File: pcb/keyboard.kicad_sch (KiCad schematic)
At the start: 52 parts, among them J1 TRRS, SW11 11, SW12 12, SW13 13, SW14 14, SW15 15, SW16 16, SW17 17, SW18 18, SW19 19, SW21 21, SW22 22, SW23 23, SW24 24, SW25 25, SW26 26, SW27 27, SW28 28, SW29 29, SW31 31, SW32 32, SW33 33, SW34 34, SW35 35, SW36 36, SW37 37, SW38 38, SW39 39, SW41 41, SW42 42, SW43 43, SW45 45, SW46 46, SW47 47, SW48 48, SW49 49, U1 EliteC

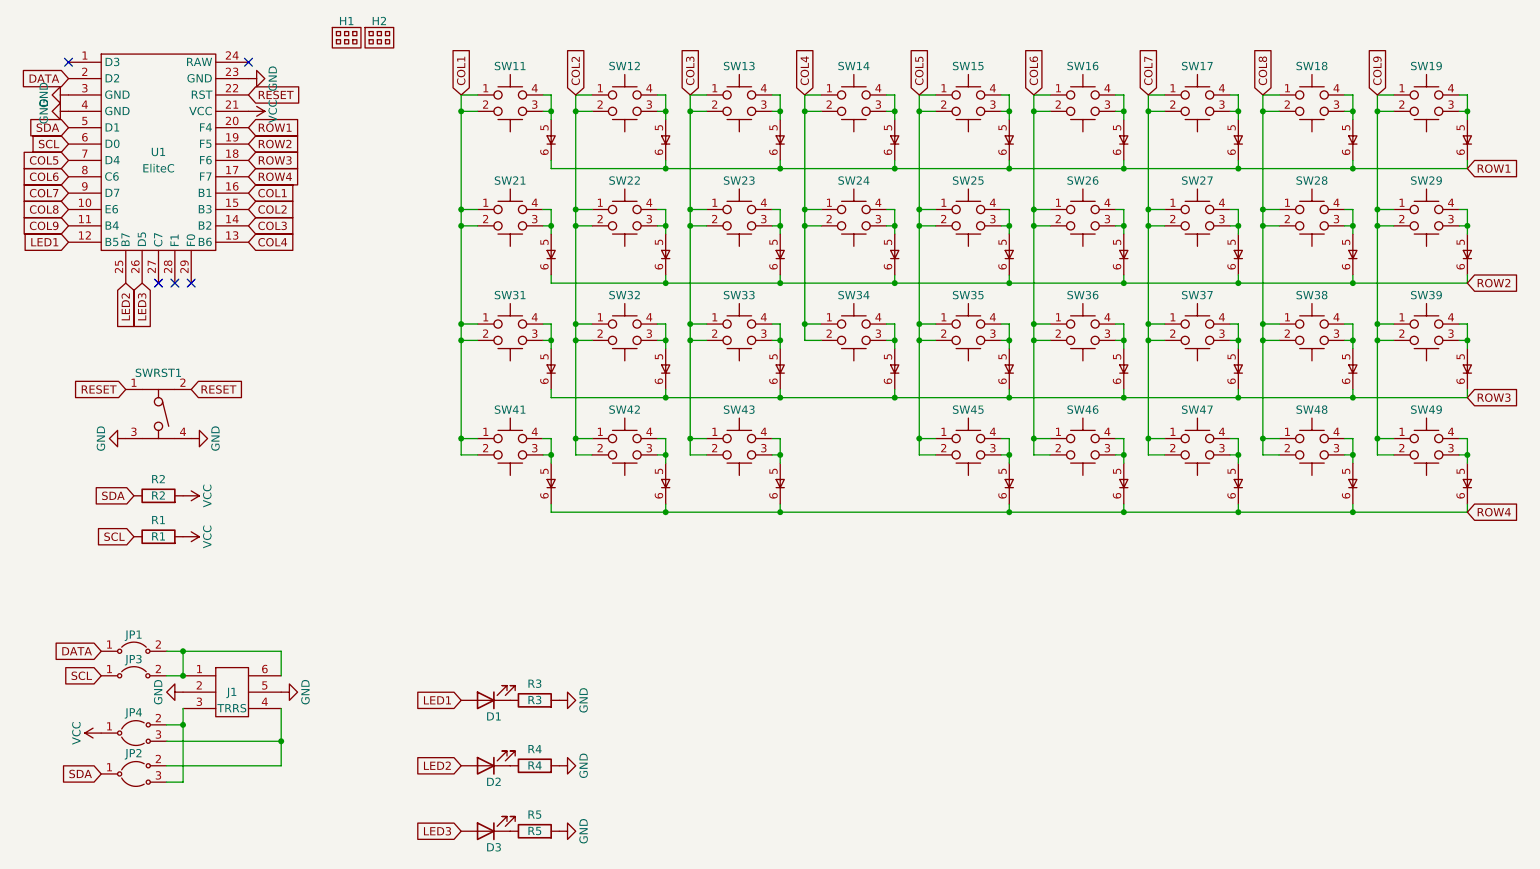
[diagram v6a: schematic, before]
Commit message: update toggling 3D model for left and right sides
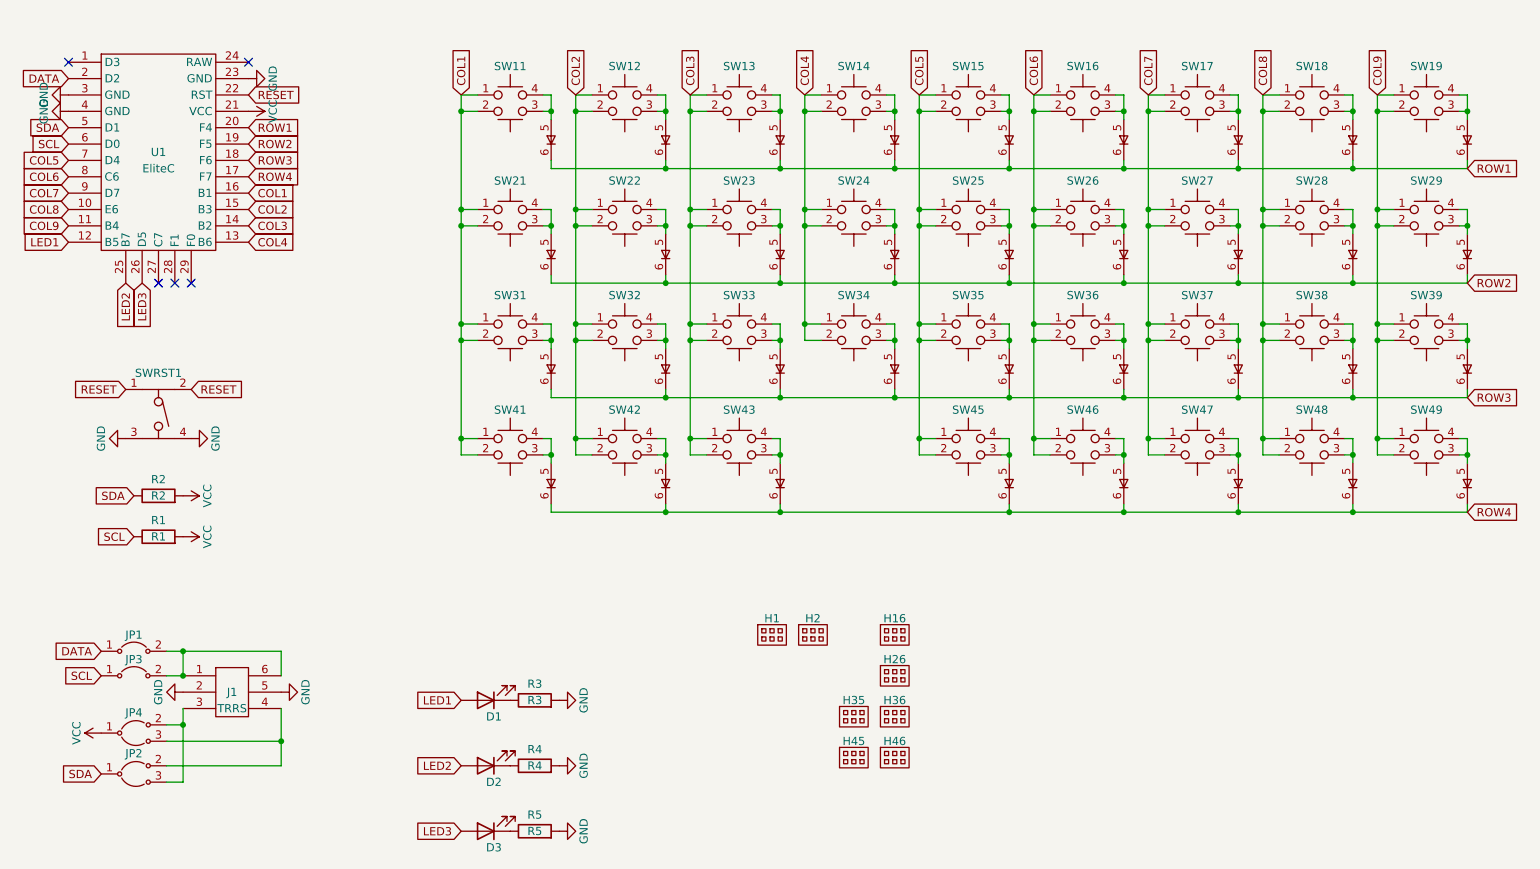
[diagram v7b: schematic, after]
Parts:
- added H16: H16, Keyboard:SwitchDoubleNo3D, symbol Keyboard:Plate
- added H26: H26, Keyboard:SwitchDoubleNo3D, symbol Keyboard:Plate
- added H35: H35, Keyboard:SwitchDoubleNo3D, symbol Keyboard:Plate
- added H36: H36, Keyboard:SwitchDoubleNo3D, symbol Keyboard:Plate
- added H45: H45, Keyboard:SwitchDoubleNo3D, symbol Keyboard:Plate
- added H46: H46, Keyboard:SwitchDoubleNo3D, symbol Keyboard:Plate
- H2: value H1 -> H2
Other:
- moved on the sheet: H1, H2
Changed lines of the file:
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@@
     )
   )
-  (symbol (lib_id "Keyboard:Plate") (at 85.09 30.48 0) (unit 1)
-    (in_bom yes) (on_board yes) (dnp no) (fields_autoplaced)
-    (property "Reference" "H1" (at 85.09 27.94 0) (do_not_autoplace)
-      (effects (font (size 1.27 1.27)))
-    )
-    (property "Value" "H1" (at 84.1375 30.1625 0) (do_not_autoplace)
-      (effects (font (size 1.27 1.27)) hide)
-    )
-    (property "Footprint" "Keyboard:RightPlate" (at 84.1375 30.1625 0)
-      (effects (font (size 1.27 1.27)) hide)
-    )
-    (property "Datasheet" "" (at 84.1375 30.1625 0)
+  (symbol (lib_id "Keyboard:Plate") (at 151.13 123.19 0) (unit 1)
+    (in_bom yes) (on_board yes) (dnp no) (fields_autoplaced)
+    (property "Reference" "H1" (at 151.13 120.65 0) (do_not_autoplace)
+      (effects (font (size 1.27 1.27)))
+    )
+    (property "Value" "H1" (at 150.1775 122.8725 0) (do_not_autoplace)
+      (effects (font (size 1.27 1.27)) hide)
+    )
+    (property "Footprint" "Keyboard:RightPlate" (at 150.1775 122.8725 0)
+      (effects (font (size 1.27 1.27)) hide)
+    )
+    (property "Datasheet" "" (at 150.1775 122.8725 0)
       (effects (font (size 1.27 1.27)) hide)
     )
@@
     )
   )
+  (symbol (lib_id "Keyboard:Plate") (at 170.18 142.24 0) (unit 1)
+    (in_bom yes) (on_board yes) (dnp no) (fields_autoplaced)
+    (property "Reference" "H46" (at 170.18 139.7 0) (do_not_autoplace)
+      (effects (font (size 1.27 1.27)))
+    )
+    (property "Value" "H46" (at 169.2275 141.9225 0) (do_not_autoplace)
+      (effects (font (size 1.27 1.27)) hide)
+    )
+    (property "Footprint" "Keyboard:SwitchDoubleNo3D" (at 169.2275 141.9225 0)
+      (effects (font (size 1.27 1.27)) hide)
+    )
+    (property "Datasheet" "" (at 169.2275 141.9225 0)
+      (effects (font (size 1.27 1.27)) hide)
+    )
+    (instances
+      (project "keyboard"
+        (path "/7807834d-3d77-4d25-b9d8-d933072c7b84"
+          (reference "H46") (unit 1)
+        )
+      )
+    )
+  )
   (symbol (lib_id "Keyboard:Switch") (at 217.17 40.64 0) (unit 1)
     (in_bom yes) (on_board yes) (dnp no) (fields_autoplaced)
@@
     )
   )
+  (symbol (lib_id "Keyboard:Plate") (at 170.18 123.19 0) (unit 1)
+    (in_bom yes) (on_board yes) (dnp no) (fields_autoplaced)
+    (property "Reference" "H16" (at 170.18 120.65 0) (do_not_autoplace)
+      (effects (font (size 1.27 1.27)))
+    )
+    (property "Value" "H16" (at 169.2275 122.8725 0) (do_not_autoplace)
+      (effects (font (size 1.27 1.27)) hide)
+    )
+    (property "Footprint" "Keyboard:SwitchDoubleNo3D" (at 169.2275 122.8725 0)
+      (effects (font (size 1.27 1.27)) hide)
+    )
+    (property "Datasheet" "" (at 169.2275 122.8725 0)
+      (effects (font (size 1.27 1.27)) hide)
+    )
+    (instances
+      (project "keyboard"
+        (path "/7807834d-3d77-4d25-b9d8-d933072c7b84"
+          (reference "H16") (unit 1)
+        )
+      )
+    )
+  )
   (symbol (lib_id "Keyboard:Switch") (at 199.39 76.2 0) (unit 1)
     (in_bom yes) (on_board yes) (dnp no) (fields_autoplaced)
@@
     )
   )
+  (symbol (lib_id "Keyboard:Plate") (at 163.83 135.89 0) (unit 1)
+    (in_bom yes) (on_board yes) (dnp no) (fields_autoplaced)
+    (property "Reference" "H35" (at 163.83 133.35 0) (do_not_autoplace)
+      (effects (font (size 1.27 1.27)))
+    )
+    (property "Value" "H35" (at 162.8775 135.5725 0) (do_not_autoplace)
+      (effects (font (size 1.27 1.27)) hide)
+    )
+    (property "Footprint" "Keyboard:SwitchDoubleNo3D" (at 162.8775 135.5725 0)
+      (effects (font (size 1.27 1.27)) hide)
+    )
+    (property "Datasheet" "" (at 162.8775 135.5725 0)
+      (effects (font (size 1.27 1.27)) hide)
+    )
+    (instances
+      (project "keyboard"
+        (path "/7807834d-3d77-4d25-b9d8-d933072c7b84"
+          (reference "H35") (unit 1)
+        )
+      )
+    )
+  )
+  (symbol (lib_id "Keyboard:Plate") (at 170.18 135.89 0) (unit 1)
+    (in_bom yes) (on_board yes) (dnp no) (fields_autoplaced)
+    (property "Reference" "H36" (at 170.18 133.35 0) (do_not_autoplace)
+      (effects (font (size 1.27 1.27)))
+    )
+    (property "Value" "H36" (at 169.2275 135.5725 0) (do_not_autoplace)
+      (effects (font (size 1.27 1.27)) hide)
+    )
+    (property "Footprint" "Keyboard:SwitchDoubleNo3D" (at 169.2275 135.5725 0)
+      (effects (font (size 1.27 1.27)) hide)
+    )
+    (property "Datasheet" "" (at 169.2275 135.5725 0)
+      (effects (font (size 1.27 1.27)) hide)
+    )
+    (instances
+      (project "keyboard"
+        (path "/7807834d-3d77-4d25-b9d8-d933072c7b84"
+          (reference "H36") (unit 1)
+        )
+      )
+    )
+  )
   (symbol (lib_id "power:GND") (at 41.91 39.37 270) (unit 1)
     (in_bom yes) (on_board yes) (dnp no) (fields_autoplaced)
@@
     )
   )
-  (symbol (lib_id "Keyboard:Plate") (at 90.17 30.48 0) (unit 1)
-    (in_bom yes) (on_board yes) (dnp no) (fields_autoplaced)
-    (property "Reference" "H2" (at 90.17 27.94 0) (do_not_autoplace)
-      (effects (font (size 1.27 1.27)))
-    )
-    (property "Value" "H1" (at 89.2175 30.1625 0) (do_not_autoplace)
-      (effects (font (size 1.27 1.27)) hide)
-    )
-    (property "Footprint" "Keyboard:LeftPlate" (at 89.2175 30.1625 0)
-      (effects (font (size 1.27 1.27)) hide)
-    )
-    (property "Datasheet" "" (at 89.2175 30.1625 0)
+  (symbol (lib_id "Keyboard:Plate") (at 157.48 123.19 0) (unit 1)
+    (in_bom yes) (on_board yes) (dnp no) (fields_autoplaced)
+    (property "Reference" "H2" (at 157.48 120.65 0) (do_not_autoplace)
+      (effects (font (size 1.27 1.27)))
+    )
+    (property "Value" "H2" (at 156.5275 122.8725 0) (do_not_autoplace)
+      (effects (font (size 1.27 1.27)) hide)
+    )
+    (property "Footprint" "Keyboard:LeftPlate" (at 156.5275 122.8725 0)
+      (effects (font (size 1.27 1.27)) hide)
+    )
+    (property "Datasheet" "" (at 156.5275 122.8725 0)
       (effects (font (size 1.27 1.27)) hide)
     )
@@
         (path "/7807834d-3d77-4d25-b9d8-d933072c7b84"
           (reference "H2") (unit 1)
+        )
+      )
+    )
+  )
+  (symbol (lib_id "Keyboard:Plate") (at 170.18 129.54 0) (unit 1)
+    (in_bom yes) (on_board yes) (dnp no) (fields_autoplaced)
+    (property "Reference" "H26" (at 170.18 127 0) (do_not_autoplace)
+      (effects (font (size 1.27 1.27)))
+    )
+    (property "Value" "H26" (at 169.2275 129.2225 0) (do_not_autoplace)
+      (effects (font (size 1.27 1.27)) hide)
+    )
+    (property "Footprint" "Keyboard:SwitchDoubleNo3D" (at 169.2275 129.2225 0)
+      (effects (font (size 1.27 1.27)) hide)
+    )
+    (property "Datasheet" "" (at 169.2275 129.2225 0)
+      (effects (font (size 1.27 1.27)) hide)
+    )
+    (instances
+      (project "keyboard"
+        (path "/7807834d-3d77-4d25-b9d8-d933072c7b84"
+          (reference "H26") (unit 1)
         )
       )
@@
         )
       )
+    )
+  )
+  (symbol (lib_id "Keyboard:Plate") (at 163.83 142.24 0) (unit 1)
+    (in_bom yes) (on_board yes) (dnp no) (fields_autoplaced)
+    (property "Reference" "H45" (at 163.83 139.7 0) (do_not_autoplace)
+      (effects (font (size 1.27 1.27)))
+    )
+    (property "Value" "H45" (at 162.8775 141.9225 0) (do_not_autoplace)
+      (effects (font (size 1.27 1.27)) hide)
+    )
+    (property "Footprint" "Keyboard:SwitchDoubleNo3D" (at 162.8775 141.9225 0)
+      (effects (font (size 1.27 1.27)) hide)
+    )
+    (property "Datasheet" "" (at 162.8775 141.9225 0)
+      (effects (font (size 1.27 1.27)) hide)
+    )
+    (instances
+      (project "keyboard"
+        (path "/7807834d-3d77-4d25-b9d8-d933072c7b84"
+          (reference "H45") (unit 1)
+        )
+      )

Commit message: fix LED footprint name and type
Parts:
- D1, D2, D3: footprint Keyboard:LED -> Keyboard:HLMP-1401
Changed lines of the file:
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@@
       (effects (font (size 1.27 1.27)) hide)
     )
-    (property "Footprint" "Keyboard:LED" (at 106.68 143.51 0)
+    (property "Footprint" "Keyboard:HLMP-1401" (at 106.68 143.51 0)
       (effects (font (size 1.27 1.27)) hide)
     )
@@
       (effects (font (size 1.27 1.27)) hide)
     )
-    (property "Footprint" "Keyboard:LED" (at 106.68 153.67 0)
+    (property "Footprint" "Keyboard:HLMP-1401" (at 106.68 153.67 0)
       (effects (font (size 1.27 1.27)) hide)
     )
@@
       (effects (font (size 1.27 1.27)) hide)
     )
-    (property "Footprint" "Keyboard:LED" (at 106.68 133.35 0)
-      (effects (font (size 1.27 1.27)) hide)
-    )
+    (property "Footprint" "Keyboard:HLMP-1401" (at 106.68 133.35 0)
+      (effects (font (size 1.27 1.27)) hide)
+    )
